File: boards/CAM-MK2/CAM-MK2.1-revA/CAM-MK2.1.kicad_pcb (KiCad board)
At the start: 4 copper layers, 40 x 40 mm, 115 parts, among them J101 USB4105-GF-A, J102 2157601002, J103 Conn_01x03, J104 Conn_01x05, J105 Conn_01x03, J106 Conn_01x05, J107 Conn_01x03, J108 Conn_01x03, J109 Conn_01x03, U101 ECMF02-2AMX6, U102 MCP2518FDT-xSL, U103 TPSM863252, U104 TPS61288, U105 TCAN337G, U106 INA745x, U107 ADG752BRT, U108 TPS2121, U109 ESP32-S3-MINI-1U, U111 TPS274160B, Y101 40MHz

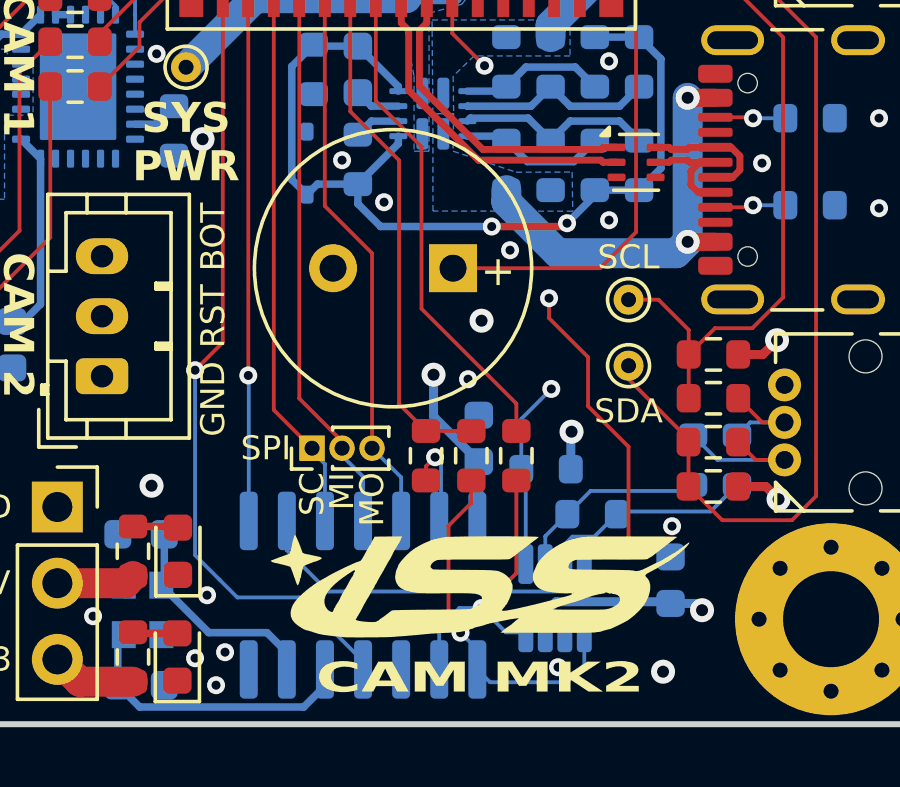
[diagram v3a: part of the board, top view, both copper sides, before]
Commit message: changed labels
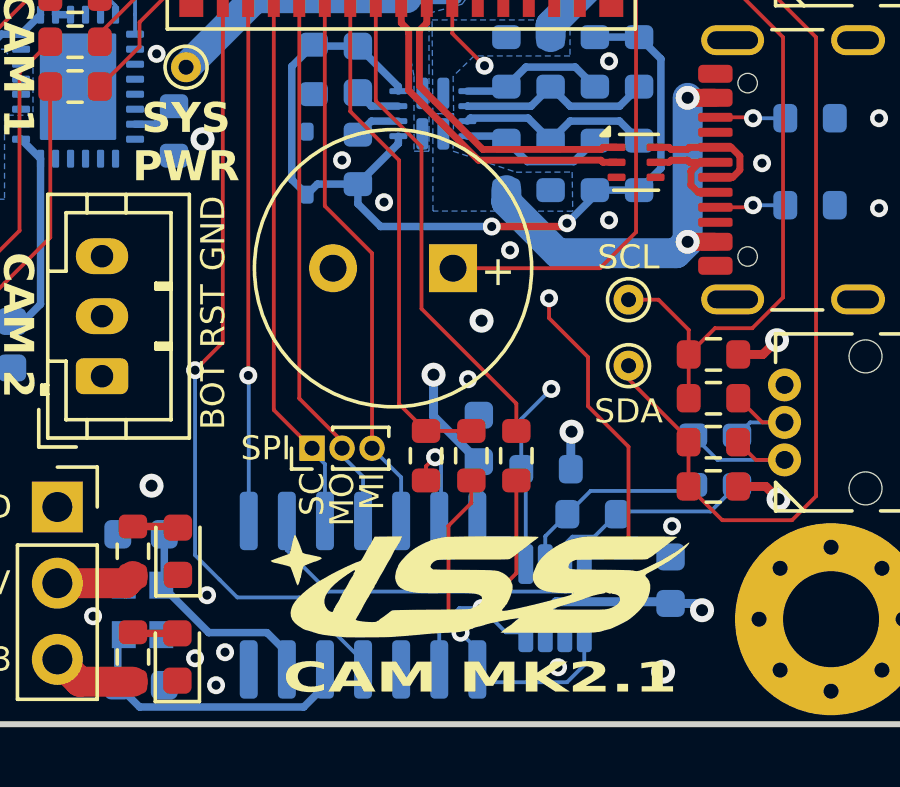
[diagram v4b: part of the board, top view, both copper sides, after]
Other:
- board text added: "CAM MK2.1"
- board text removed: "CAM MK2"
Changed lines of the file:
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@@
 	(paper "A4")
 	(title_block
-		(title "Stargazer Camera Board MK2")
+		(title "Stargazer Camera Board MK2.1")
 		(date "2024-12-01")
 		(rev "A")
@@
 	)
 	(gr_text "GND"
-		(at 143.9 97.9 -90)
+		(at 143.9 94.9 270)
 		(layer "B.SilkS")
 		(effects
@@
 				(thickness 0.15)
 			)
-			(justify right mirror)
+			(justify left mirror)
 		)
 	)
 	(gr_text "MOSI"
-		(at 151.2 100.2 -90)
+		(at 150.2 100.2 -90)
 		(layer "B.SilkS")
 		(effects
@@
 	)
 	(gr_text "BOT"
-		(at 143.9 94.9 -90)
+		(at 143.9 97.9 270)
 		(layer "B.SilkS")
 		(effects
@@
 				(thickness 0.15)
 			)
-			(justify left mirror)
+			(justify right mirror)
 		)
 	)
 	(gr_text "MISO"
-		(at 150.2 100.2 -90)
+		(at 151.2 100.2 -90)
 		(layer "B.SilkS")
 		(effects
@@
 		)
 	)
-	(gr_text "CAM MK2"
+	(gr_text "CAM MK2.1"
 		(at 154.8 108.45 0)
 		(layer "F.SilkS")
@@
 			)
 		)
-		(render_cache "CAM MK2" 0
+		(render_cache "CAM MK2.1" 0
+			(polygon
+				(pts
+					(xy 151.998046 108.779759) (xy 151.980643 108.828289) (xy 151.921961 108.858257) (xy 151.850767 108.865)
+					(xy 151.347749 108.865) (xy 151.272208 108.856675) (xy 151.215832 108.820964) (xy 151.204501 108.779759)
+					(xy 151.204501 107.871664) (xy 151.221427 107.823133) (xy 151.285078 107.791751) (xy 151.347749 107.786423)
+					(xy 151.850767 107.786423) (xy 151.928434 107.794747) (xy 151.986396 107.830459) (xy 151.998046 107.871664)
+					(xy 151.998046 108.145949) (xy 151.758077 108.145949) (xy 151.758077 107.942739) (xy 151.445935 107.942739)
+					(xy 151.445935 108.708684) (xy 151.758077 108.708684) (xy 151.758077 108.505474) (xy 151.998046 108.505474)
+				)
+			)
+			(polygon
+				(pts
+					(xy 152.999319 108.865) (xy 152.760083 108.865) (xy 152.711723 108.677421) (xy 152.409839 108.677421)
+					(xy 152.361479 108.865) (xy 152.123342 108.865) (xy 152.123342 108.862313) (xy 152.222335 108.521106)
+					(xy 152.441713 108.521106) (xy 152.677651 108.521106) (xy 152.560415 108.035795) (xy 152.441713 108.521106)
+					(xy 152.222335 108.521106) (xy 152.435485 107.786423) (xy 152.689009 107.786423)
+				)
+			)
 			(polygon
 				(pts
-					(xy 152.436951 108.779759) (xy 152.419548 108.828289) (xy 152.360866 108.858257) (xy 152.289672 108.865)
-					(xy 151.786654 108.865) (xy 151.711113 108.856675) (xy 151.654737 108.820964) (xy 151.643406 108.779759)
-					(xy 151.643406 107.871664) (xy 151.660332 107.823133) (xy 151.723983 107.791751) (xy 151.786654 107.786423)
-					(xy 152.289672 107.786423) (xy 152.367339 107.794747) (xy 152.425301 107.830459) (xy 152.436951 107.871664)
-					(xy 152.436951 108.145949) (xy 152.196982 108.145949) (xy 152.196982 107.942739) (xy 151.88484 107.942739)
-					(xy 151.88484 108.708684) (xy 152.196982 108.708684) (xy 152.196982 108.505474) (xy 152.436951 108.505474)
+					(xy 154.103541 108.865) (xy 153.871633 108.865) (xy 153.871633 108.328886) (xy 153.875296 108.278267)
+					(xy 153.882852 108.229323) (xy 153.886287 108.210917) (xy 153.677826 108.755579) (xy 153.55546 108.755579)
+					(xy 153.346266 108.210917) (xy 153.354401 108.259679) (xy 153.359871 108.3093) (xy 153.360554 108.328886)
+					(xy 153.360554 108.865) (xy 153.128646 108.865) (xy 153.128646 107.786423) (xy 153.356524 107.786423)
+					(xy 153.610048 108.376025) (xy 153.616277 108.424385) (xy 153.622505 108.376025) (xy 153.875663 107.786423)
+					(xy 154.103541 107.786423)
 				)
 			)
 			(polygon
 				(pts
-					(xy 153.438224 108.865) (xy 153.198988 108.865) (xy 153.150628 108.677421) (xy 152.848744 108.677421)
-					(xy 152.800384 108.865) (xy 152.562247 108.865) (xy 152.562247 108.862313) (xy 152.66124 108.521106)
-					(xy 152.880618 108.521106) (xy 153.116556 108.521106) (xy 152.99932 108.035795) (xy 152.880618 108.521106)
-					(xy 152.66124 108.521106) (xy 152.87439 107.786423) (xy 153.127914 107.786423)
+					(xy 155.696493 108.865) (xy 155.464584 108.865) (xy 155.464584 108.328886) (xy 155.468248 108.278267)
+					(xy 155.475804 108.229323) (xy 155.479239 108.210917) (xy 155.270778 108.755579) (xy 155.148412 108.755579)
+					(xy 154.939218 108.210917) (xy 154.947353 108.259679) (xy 154.952823 108.3093) (xy 154.953506 108.328886)
+					(xy 154.953506 108.865) (xy 154.721598 108.865) (xy 154.721598 107.786423) (xy 154.949476 107.786423)
+					(xy 155.203 108.376025) (xy 155.209229 108.424385) (xy 155.215457 108.376025) (xy 155.468614 107.786423)
+					(xy 155.696493 107.786423)
 				)
 			)
 			(polygon
 				(pts
-					(xy 154.542446 108.865) (xy 154.310538 108.865) (xy 154.310538 108.328886) (xy 154.314201 108.278267)
-					(xy 154.321757 108.229323) (xy 154.325192 108.210917) (xy 154.116731 108.755579) (xy 153.994365 108.755579)
-					(xy 153.785171 108.210917) (xy 153.793306 108.259679) (xy 153.798776 108.3093) (xy 153.799459 108.328886)
-					(xy 153.799459 108.865) (xy 153.567551 108.865) (xy 153.567551 107.786423) (xy 153.795429 107.786423)
-					(xy 154.048953 108.376025) (xy 154.055182 108.424385) (xy 154.06141 108.376025) (xy 154.314568 107.786423)
-					(xy 154.542446 107.786423)
+					(xy 156.695202 108.865) (xy 156.429588 108.865) (xy 156.123674 108.387749) (xy 156.123674 108.865)
+					(xy 155.88224 108.865) (xy 155.88224 107.786423) (xy 156.123674 107.786423) (xy 156.123674 108.246821)
+					(xy 156.391486 107.786423) (xy 156.655268 107.786423) (xy 156.655268 107.793995) (xy 156.327372 108.31008)
 				)
 			)
 			(polygon
 				(pts
-					(xy 156.135398 108.865) (xy 155.903489 108.865) (xy 155.903489 108.328886) (xy 155.907153 108.278267)
-					(xy 155.914709 108.229323) (xy 155.918144 108.210917) (xy 155.709683 108.755579) (xy 155.587317 108.755579)
-					(xy 155.378123 108.210917) (xy 155.386258 108.259679) (xy 155.391728 108.3093) (xy 155.392411 108.328886)
-					(xy 155.392411 108.865) (xy 155.160503 108.865) (xy 155.160503 107.786423) (xy 155.388381 107.786423)
-					(xy 155.641905 108.376025) (xy 155.648134 108.424385) (xy 155.654362 108.376025) (xy 155.907519 107.786423)
-					(xy 156.135398 107.786423)
+					(xy 157.544068 108.080247) (xy 157.532557 108.13029) (xy 157.503957 108.177567) (xy 157.491678 108.192843)
+					(xy 157.048377 108.708684) (xy 157.54187 108.708684) (xy 157.54187 108.865) (xy 156.759682 108.865)
+					(xy 156.759682 108.763394) (xy 157.305931 108.123234) (xy 157.305931 107.942739) (xy 157.012107 107.942739)
+					(xy 157.012107 108.130317) (xy 156.776168 108.130317) (xy 156.776168 107.871664) (xy 156.793572 107.823133)
+					(xy 156.852253 107.793166) (xy 156.923447 107.786423) (xy 157.396423 107.786423) (xy 157.474283 107.794747)
+					(xy 157.532389 107.830459) (xy 157.544068 107.871664)
 				)
 			)
 			(polygon
 				(pts
-					(xy 157.134107 108.865) (xy 156.868493 108.865) (xy 156.562579 108.387749) (xy 156.562579 108.865)
-					(xy 156.321145 108.865) (xy 156.321145 107.786423) (xy 156.562579 107.786423) (xy 156.562579 108.246821)
-					(xy 156.830391 107.786423) (xy 157.094173 107.786423) (xy 157.094173 107.793995) (xy 156.766277 108.31008)
+					(xy 157.92472 108.865) (xy 157.692812 108.865) (xy 157.692812 108.693053) (xy 157.92472 108.693053)
 				)
 			)
 			(polygon
 				(pts
-					(xy 157.982973 108.080247) (xy 157.971462 108.13029) (xy 157.942862 108.177567) (xy 157.930583 108.192843)
-					(xy 157.487282 108.708684) (xy 157.980775 108.708684) (xy 157.980775 108.865) (xy 157.198587 108.865)
-					(xy 157.198587 108.763394) (xy 157.744836 108.123234) (xy 157.744836 107.942739) (xy 157.451012 107.942739)
-					(xy 157.451012 108.130317) (xy 157.215073 108.130317) (xy 157.215073 107.871664) (xy 157.232477 107.823133)
-					(xy 157.291158 107.793166) (xy 157.362352 107.786423) (xy 157.835328 107.786423) (xy 157.913188 107.794747)
-					(xy 157.971294 107.830459) (xy 157.982973 107.871664)
+					(xy 158.388171 108.865) (xy 158.151134 108.865) (xy 158.151134 108.099054) (xy 158.058443 108.099054)
+					(xy 158.058443 108.075607) (xy 158.183374 107.786423) (xy 158.388171 107.786423)
 				)
 			)
@@
 	)
 	(gr_text "GND"
-		(at 145.9 97.9 90)
+		(at 145.9 94.9 90)
 		(layer "F.SilkS")
 		(effects
@@
 				(thickness 0.15)
 			)
-			(justify right)
+			(justify left)
 		)
 	)
@@
 	)
 	(gr_text "MI"
-		(at 150.2 101.6 90)
+		(at 151.2 101.6 90)
 		(layer "F.SilkS")
 		(effects
@@
 	)
 	(gr_text "MO"
-		(at 151.2 101.6 90)
+		(at 150.2 101.6 90)
 		(layer "F.SilkS")
 		(effects
@@
 	)
 	(gr_text "BOT"
-		(at 145.9 94.9 90)
+		(at 145.9 97.9 90)
 		(layer "F.SilkS")
 		(effects
@@
 				(thickness 0.15)
 			)
-			(justify left)
+			(justify right)
 		)
 	)

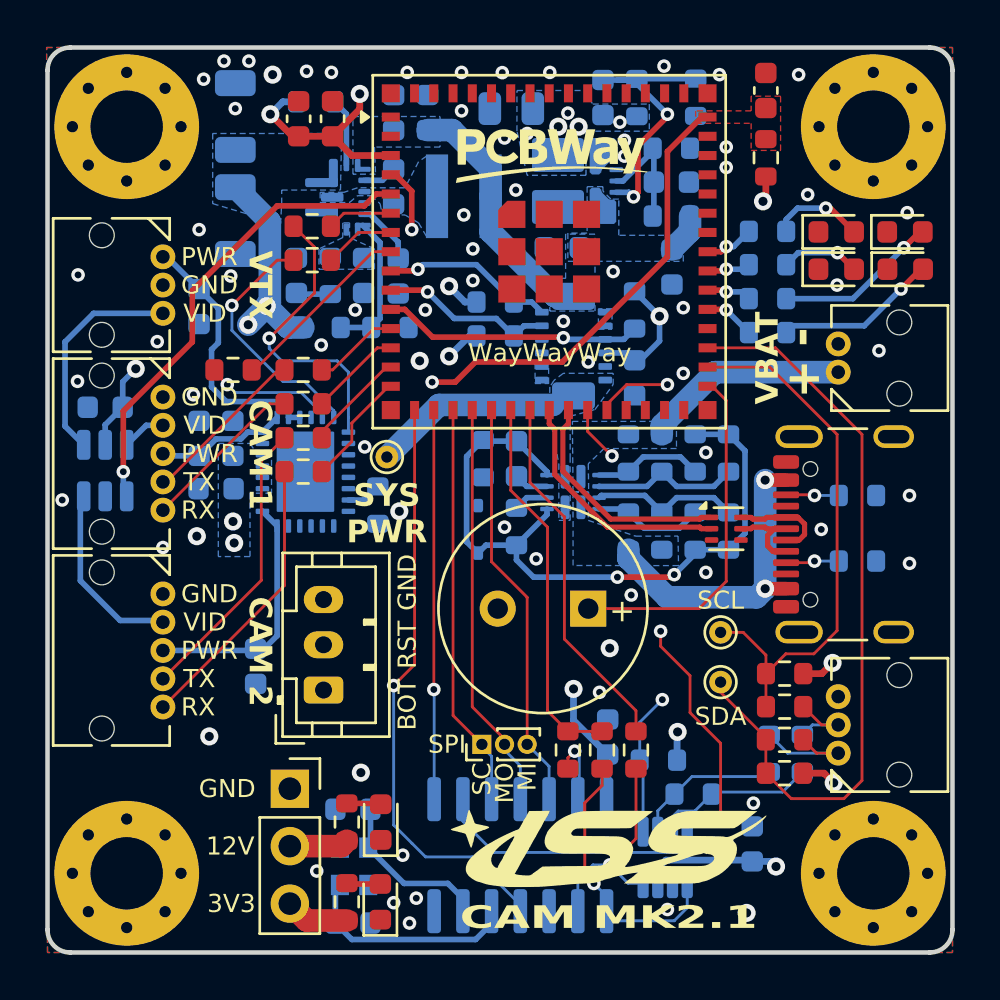
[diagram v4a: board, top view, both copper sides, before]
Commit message: Increased CAM/VTX Power Trace Widths and Reduced RST/Boot Traces on 3V3 Layer
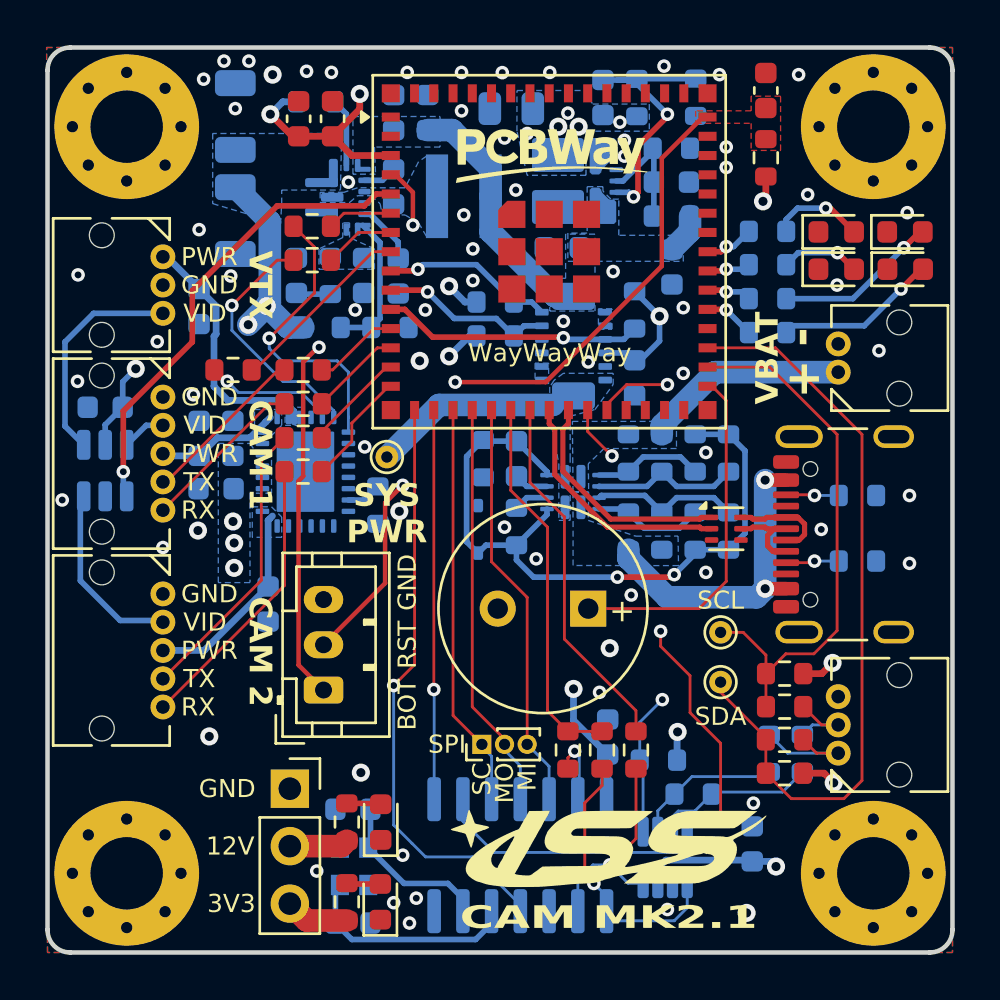
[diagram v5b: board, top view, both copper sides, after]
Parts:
- moved C125 2.80 mm to (139.8, 94.6)
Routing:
- net /CAM_2_POW: track 11.1 -> 9.02 mm
- net +12V: track 45.2 -> 47.1 mm, vias 4 -> 5
- net /RESET_SW: track 33.4 -> 32.8 mm, vias 1 -> 2
- net /BOOT_SW: track 25.8 -> 25.9 mm, vias 1 -> 2
- added copper zone on B.Cu, net /CAM_1_POW
- added copper zone on B.Cu, net /CAM_2_POW
- added copper zone on B.Cu, net /VTX_POW
